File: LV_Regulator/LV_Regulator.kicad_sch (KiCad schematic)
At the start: 36 parts, among them IC1 UCC12040DVE, K1 41.52.9.005.0010, U1 ADM2483xRW, U2 STM32F103C8Tx, U4 MCP1826T-ADJE_DC, U5 MCP1826T-ADJE_DC

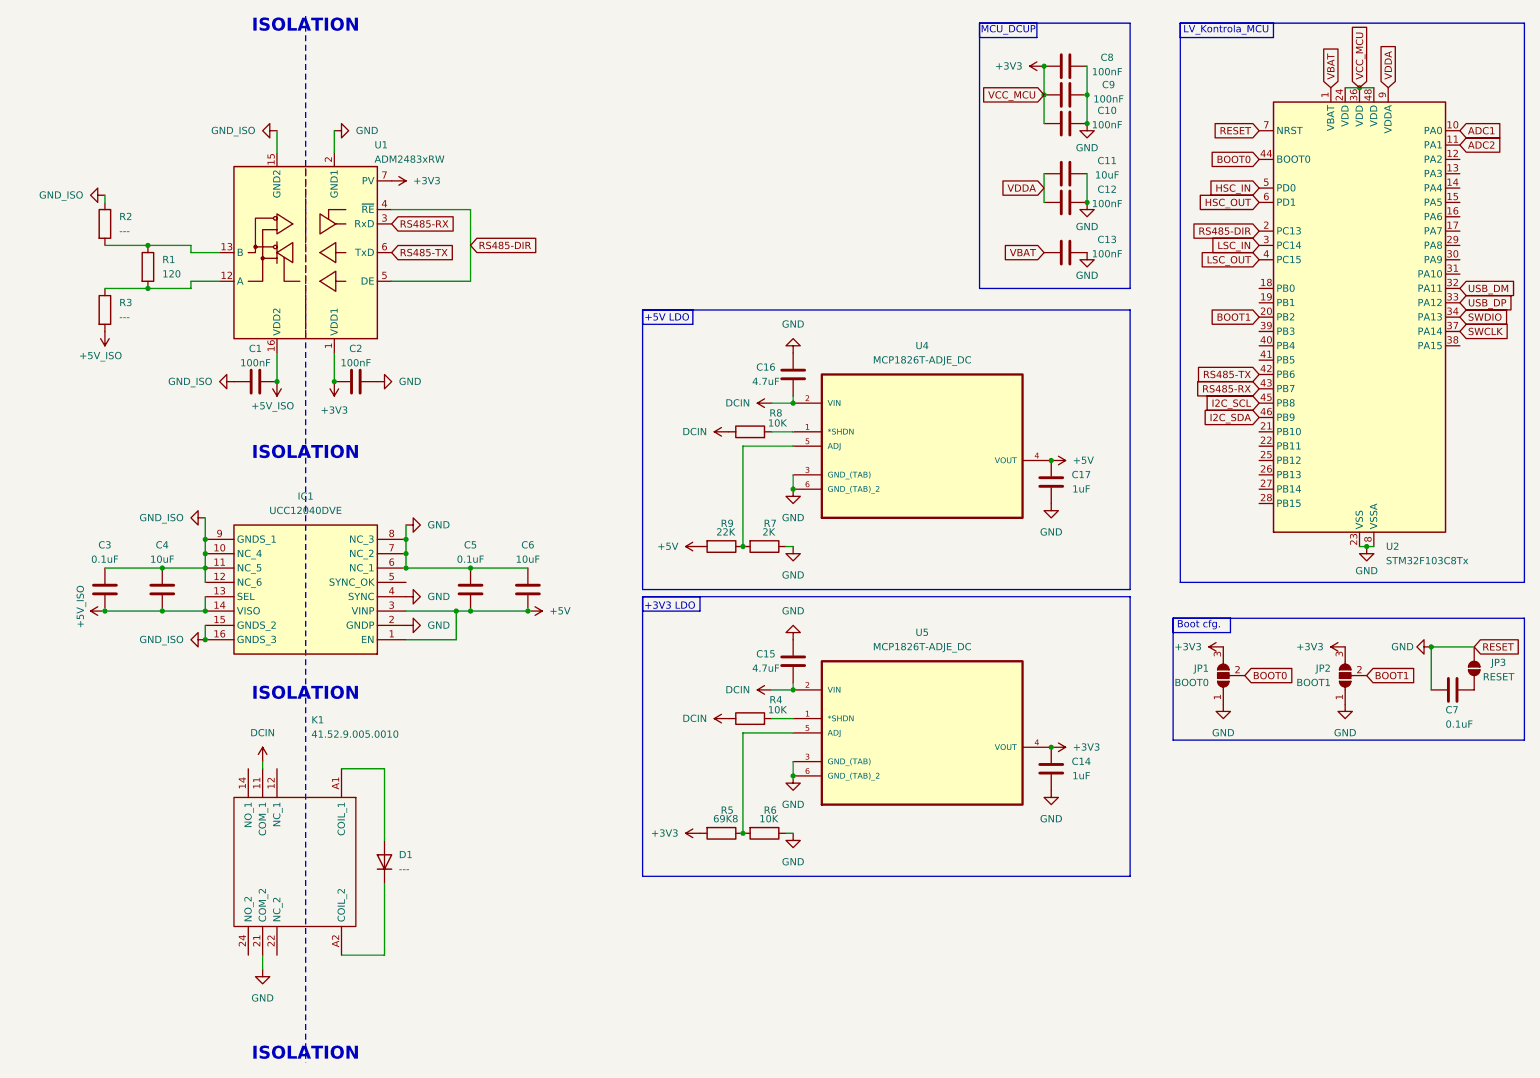
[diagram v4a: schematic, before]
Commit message: Added a lot
Created a schematic hierarchy for LV_Regulator, added connectors, added start logic, added address select jumpers for RS485, implemented start isolation on LV_Kontrola_Main,...
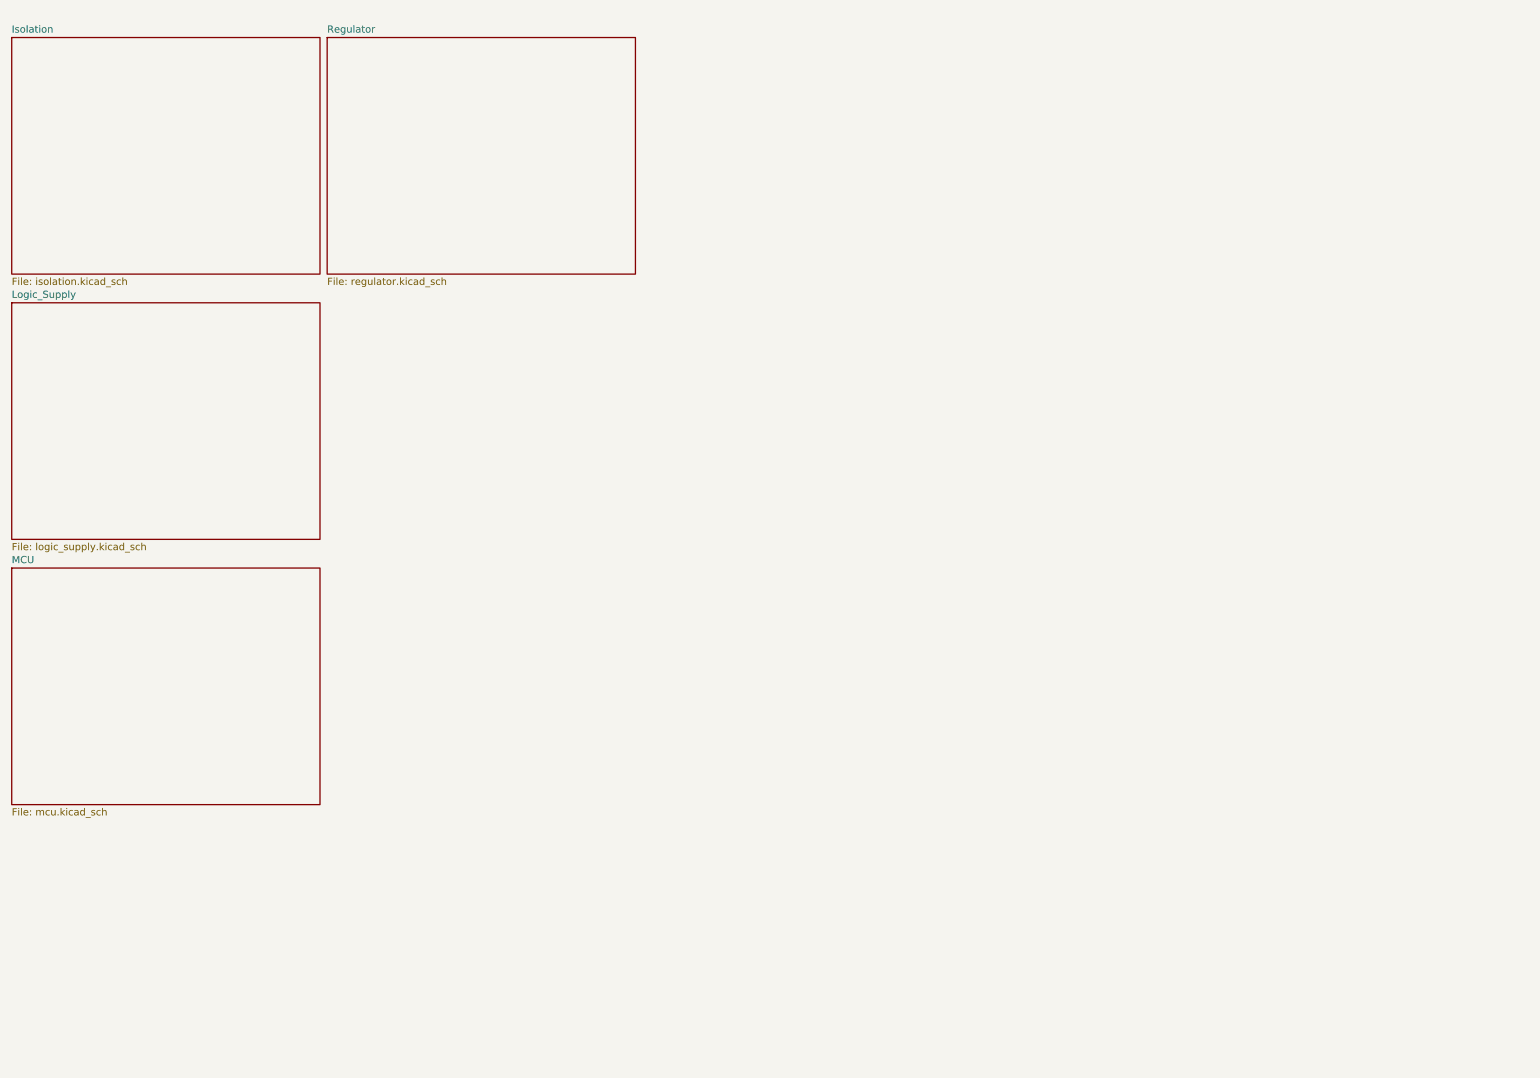
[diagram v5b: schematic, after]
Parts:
- removed C1, C10, C12, C13, C2, C8, C9: 100nF, symbol Device:C
- removed C11, C4, C6: 10uF, symbol Device:C
- removed C14, C17: 1uF, symbol Device:C
- removed C15, C16: 4.7uF, symbol Device:C
- removed C3, C5, C7: 0.1uF, symbol Device:C
- removed D1: ---, symbol Device:D
- removed IC1: UCC12040DVE, SOIC127P1030X265-16N, symbol UCC12040DVE:UCC12040DVE
- removed JP1: BOOT0, symbol Jumper:SolderJumper_3_Open
- removed JP2: BOOT1, symbol Jumper:SolderJumper_3_Open
- removed JP3: RESET, symbol Jumper:SolderJumper_2_Open
- removed K1: 41.52.9.005.0010, 415290050010, symbol 41.52.9.005.0010:41.52.9.005.0010
- removed R1: 120, symbol Device:R
- removed R2, R3: ---, symbol Device:R
- removed R4, R6, R8: 10K, symbol Device:R
- removed R5: 69K8, symbol Device:R
- removed R7: 2K, symbol Device:R
- removed R9: 22K, symbol Device:R
- removed U1: ADM2483xRW, Package_SO:SOIC-16W_7.5x10.3mm_P1.27mm, symbol Interface_UART:ADM2483xRW
- removed U2: STM32F103C8Tx, Package_QFP:LQFP-48_7x7mm_P0.5mm, symbol MCU_ST_STM32F1:STM32F103C8Tx
- removed U4, U5: MCP1826T-ADJE_DC, MCP1826T-ADJE_DC:SOT230P700X180-6N, symbol MCP1826T-ADJE_DC:MCP1826T-ADJE_DC
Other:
- added sheet Isolation (isolation.kicad_sch)
- added sheet Logic_Supply (logic_supply.kicad_sch)
- added sheet MCU (mcu.kicad_sch)
- added sheet Regulator (regulator.kicad_sch)
- note removed: "+3V3 LDO"
- note removed: "+5V LDO"
- note removed: "Boot cfg."
- note removed: "ISOLATION"
- note removed: "LV_Kontrola_MCU"
- note removed: "MCU_DCUP"

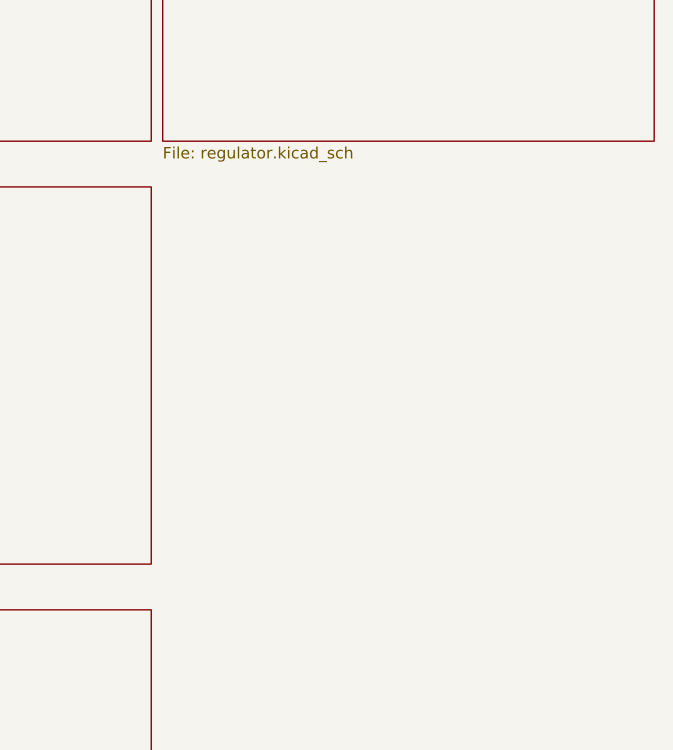
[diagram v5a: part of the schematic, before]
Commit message: Update to LV_Regulator schematic
Chosen some component's footprints as well as made a page for test points, etc.
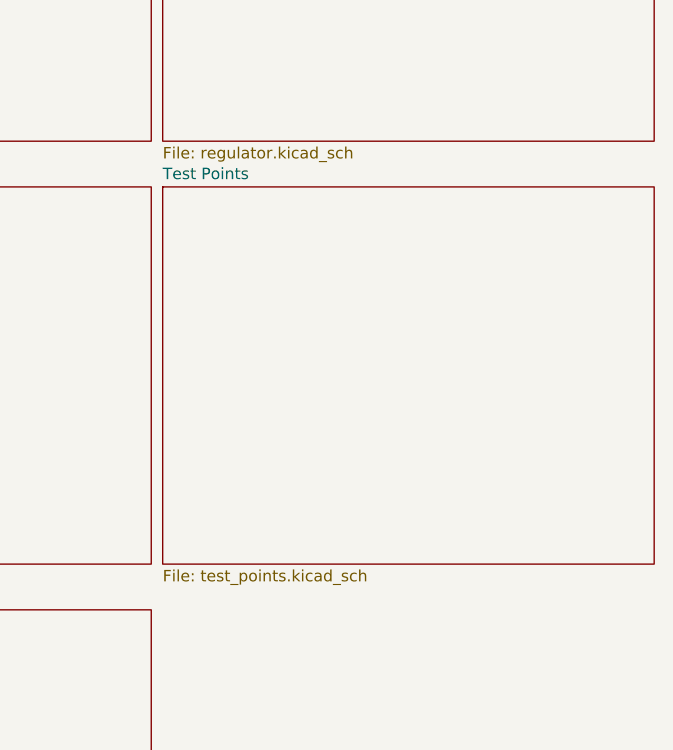
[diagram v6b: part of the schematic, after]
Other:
- added sheet Test Points (test_points.kicad_sch)
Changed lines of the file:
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@@
+	)
+	(sheet
+		(at 71.12 63.5)
+		(size 54.61 41.91)
+		(exclude_from_sim no)
+		(in_bom yes)
+		(on_board yes)
+		(dnp no)
+		(fields_autoplaced yes)
+		(stroke
+			(width 0.1524)
+			(type solid)
+		)
+		(fill
+			(color 0 0 0 0.0000)
+		)
+		(property "Sheetname" "Test Points"
+			(at 71.12 62.7884 0)
+			(effects
+				(font
+					(size 1.27 1.27)
+				)
+				(justify left bottom)
+			)
+		)
+		(property "Sheetfile" "test_points.kicad_sch"
+			(at 71.12 105.9946 0)
+			(effects
+				(font
+					(size 1.27 1.27)
+				)
+				(justify left top)
+			)
+		)
+		(instances
+			(project "LV_Regulator"
+				(path "/9003ce10-3354-47c9-924a-fd038a206791"
+					(page "6")
+				)
+			)
+		)
 	)
 	(sheet
